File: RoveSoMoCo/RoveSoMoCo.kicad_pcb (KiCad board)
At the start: 4 copper layers, 33.5 x 33.5 mm, 34 parts, among them Q1 SI4156DY, Q2 SI4156DY, Q3 SI4156DY, Q4 SI4156DY, U1 74LVC2G04, U2 IRS2005S, U3 IRS2005S, U4 74HC00

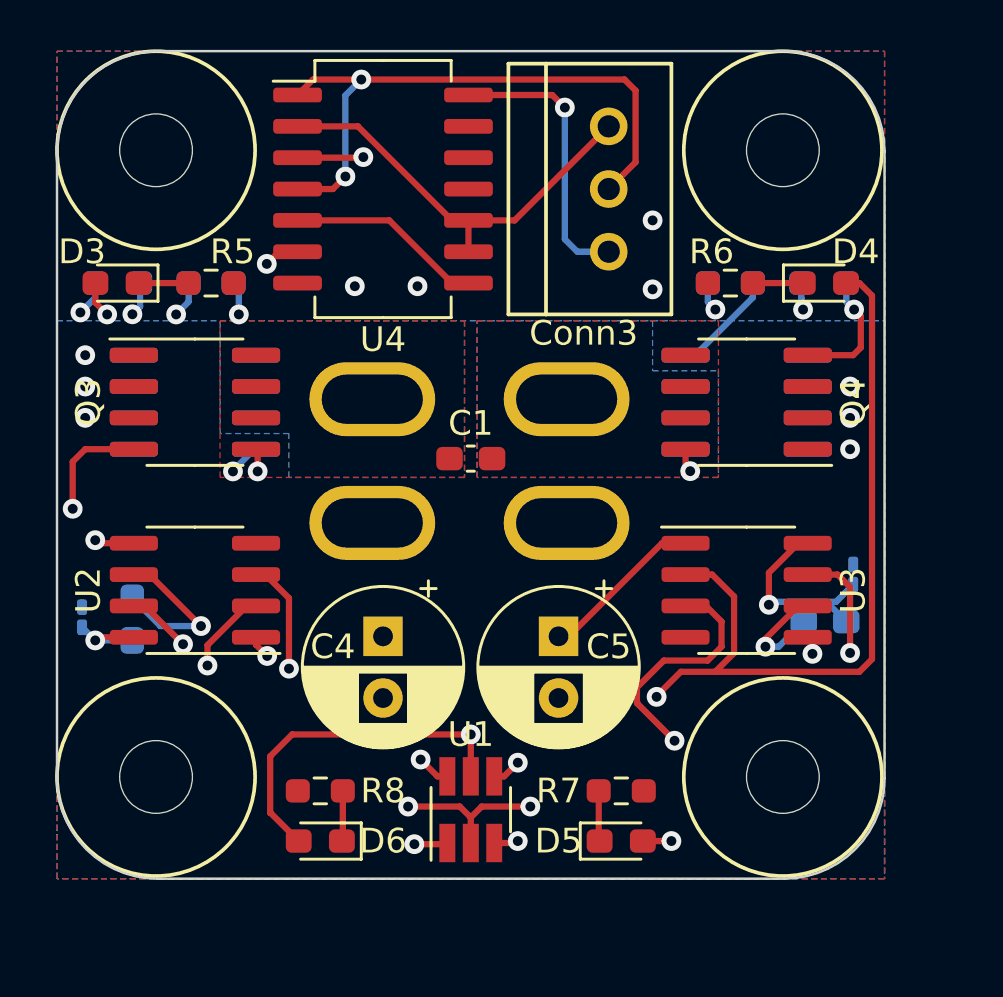
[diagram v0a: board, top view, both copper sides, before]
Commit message: Increased size of board and planes
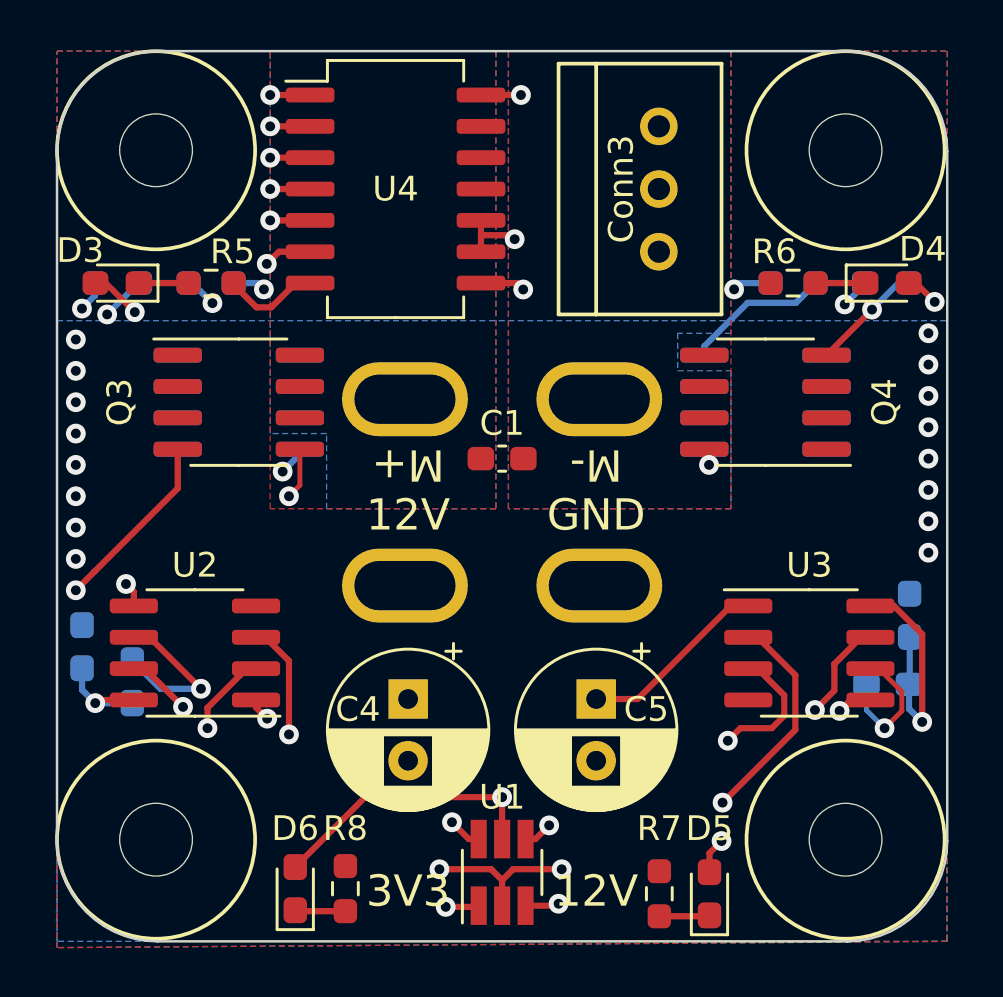
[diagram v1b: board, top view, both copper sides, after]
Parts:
- D1, D2: footprint Diode_SMD:D_0201_0603Metric_Pad0.64x0.40mm_HandSolder -> Diode_SMD:D_0603_1608Metric_Pad1.05x0.95mm_HandSolder
- moved R7 4.44 mm to (100.6, 77.3), turned to 90 degrees
- moved D5 4.16 mm to (102.6, 77.3), turned to 90 degrees
- moved R8 4.09 mm to (87.9, 77.1), turned to 90 degrees
- moved C3 3.59 mm to (109.9, 68.8)
- moved V3 3.59 mm to (104.1, 71.1)
- moved U3 3.59 mm to (106.7, 67.6)
- moved C5 2.96 mm to (98.0, 69.4)
- moved Conn2 2.86 mm to (98.7, 64.5)
- moved U1 2.84 mm to (94.2, 76.5)
- moved D2 2.82 mm to (110.7, 66.0)
- moved C4 2.74 mm to (90.4, 69.4)
- moved C2 2.54 mm to (79.2, 68.7)
- moved D4 2.54 mm to (109.8, 52.6)
- moved R2 2.54 mm to (106.0, 52.6)
- moved R6 2.54 mm to (106.0, 52.6)
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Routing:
- net /RVS: track 39.6 -> 50.7 mm, vias 2 -> 3
- net /FWD: track 38.8 -> 47.7 mm
- net PWM: track 24.9 -> 33.1 mm
- net DIR: track 17.0 -> 25.2 mm, vias 0 -> 2
- net +3V3: track 48.3 -> 56.3 mm
- net Net-(U4-Pad5): track 7.98 -> 14.8 mm, vias 0 -> 2
- net Net-(R4-Pad2): track 20.4 -> 26.3 mm
- net /M-: track 16.1 -> 21.9 mm
- net Net-(U1-Pad1): track 36.1 -> 41.6 mm
- net Net-(Q3-Pad4): track 15.9 -> 20.9 mm
- net Net-(R1-Pad1): track 20.6 -> 25.6 mm
- net /M+: track 16.0 -> 20.3 mm
- net GND: track 6.35 -> 10.3 mm, vias 12 -> 18
- net Net-(R2-Pad2): track 23.7 -> 25.7 mm
- net Net-(Q2-Pad4): track 4.28 -> 5.93 mm
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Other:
- board size 33.5 x 33.5 mm -> 36.1 x 36.1 mm
- board text added: "12V"
- board text added: "3V3"
- board text added: "GND"
- board text added: "M+"
- board text added: "M-"
